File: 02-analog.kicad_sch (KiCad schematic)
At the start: 24 parts, among them J2 Superseal_1.0_5pol_MicA, J3 Superseal_1.0_5pol_MicB

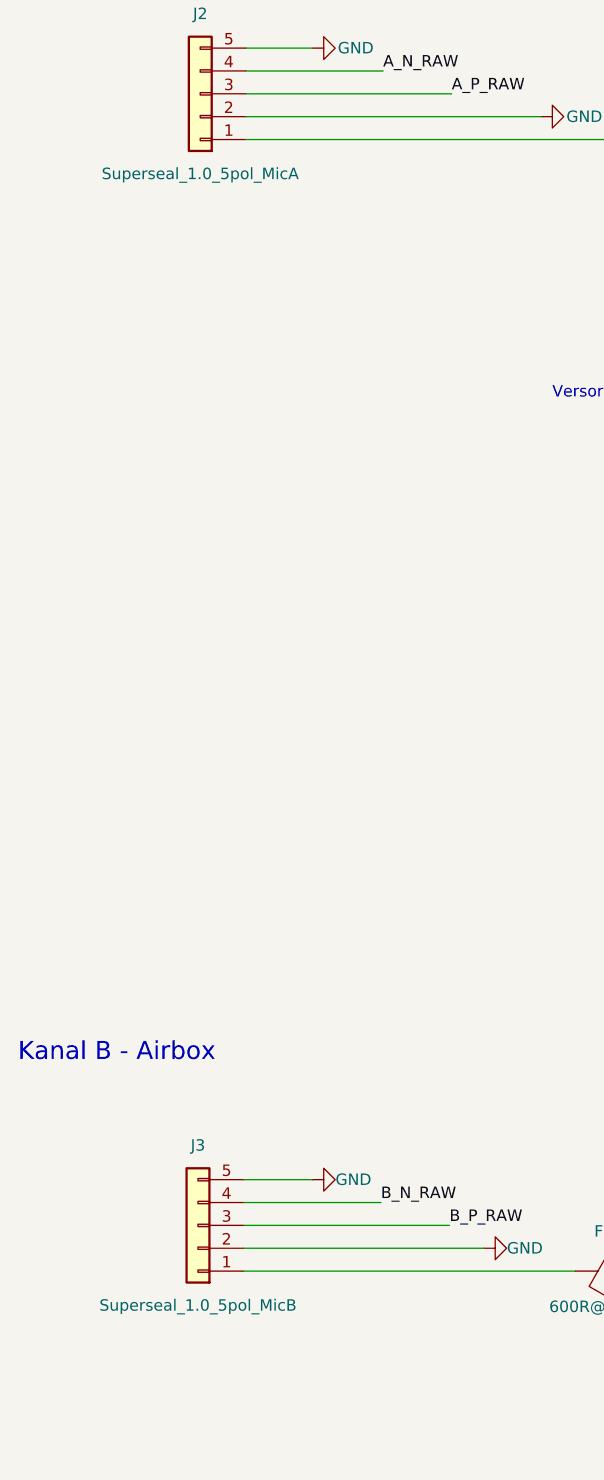
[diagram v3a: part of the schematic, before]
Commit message: Footprints im Schaltplan auf den Stand des Layouts ziehen
Neun Bauteile trugen im Schaltplan einen Footprint, der so nicht baubar ist.
Das Layout hatte sie laengst ersetzt; jetzt steht es auch im Schaltplan:

  U5      TSSOP-30 4,4 x 9,7 / 0,65  ->  4,4 x 7,8 / 0,5  (Datenblatt)
  U6      ESP32-S2-WROOM             ->  ESP32-S3-WROOM-1
  L2, L3  L_CommonModeChoke_WE-SL2   ->  L_CommonMode_WE-SL2
  J1..J3  TE Superseal 1.0           ->  JST XH liegend
  BT1     Keystone 3034 / CR2032     ->  Keystone 3000 / CR1220
  LS1     Piezo bedrahtet 12 mm      ->  Murata-Landmuster 9 x 9 mm SMD

Wo sich damit das Bauteil aendert, sind Wert und Bestellnummer mitgezogen.
Zwei Punkte dabei zum Nachlesen:

* BT1 hat mit CR1220 rund ein Viertel der Kapazitaet von CR2032. Die
  Platine ist fuer den 12-mm-Halter gebohrt, darum folgt der Schaltplan.
* Der im Layout benannte Murata PKMCS0909E ist abgekuendigt ("Last Time
  Buy") und nur fuer 1,5 V spezifiziert, angesteuert wird aber mit 3,3 V.
  Bestellt wird darum ein 3-V-Typ gleicher Bauform (Same Sky
  CPT-9019A-SMT-TR); das Landmuster gehoert gegen das Datenblatt geprueft.

Damit sind die Steckverbinder J1..J3 beschaffbar - Superseal 1.0 gibt es bei
DigiKey nur kabelseitig. Offen bleiben noch J4 und MK1.

Schaltplanparitaet: 18 -> 9 Abweichungen auf der Hauptplatine, 2 auf dem
Mikrofonkopf. Die restlichen sind keine Footprints mehr, sondern Symbole:
U2 hat einen Pin 4, den das SOT-223 nicht hat, und dem microSD-Symbol fehlt
der Schirmanschluss. Beides steht im README.

Die Stueckliste fuehrt jetzt eine Spalte Hinweis - dort landen die
Ersatzgruende, die vorher nur im Schaltplan standen.

DRC unveraendert: 0 Fehler, 10 Warnungen, 7 offene Verbindungen. ERC
unveraendert. Stuecklisten, Fertigungsdaten und PDFs neu erzeugt.
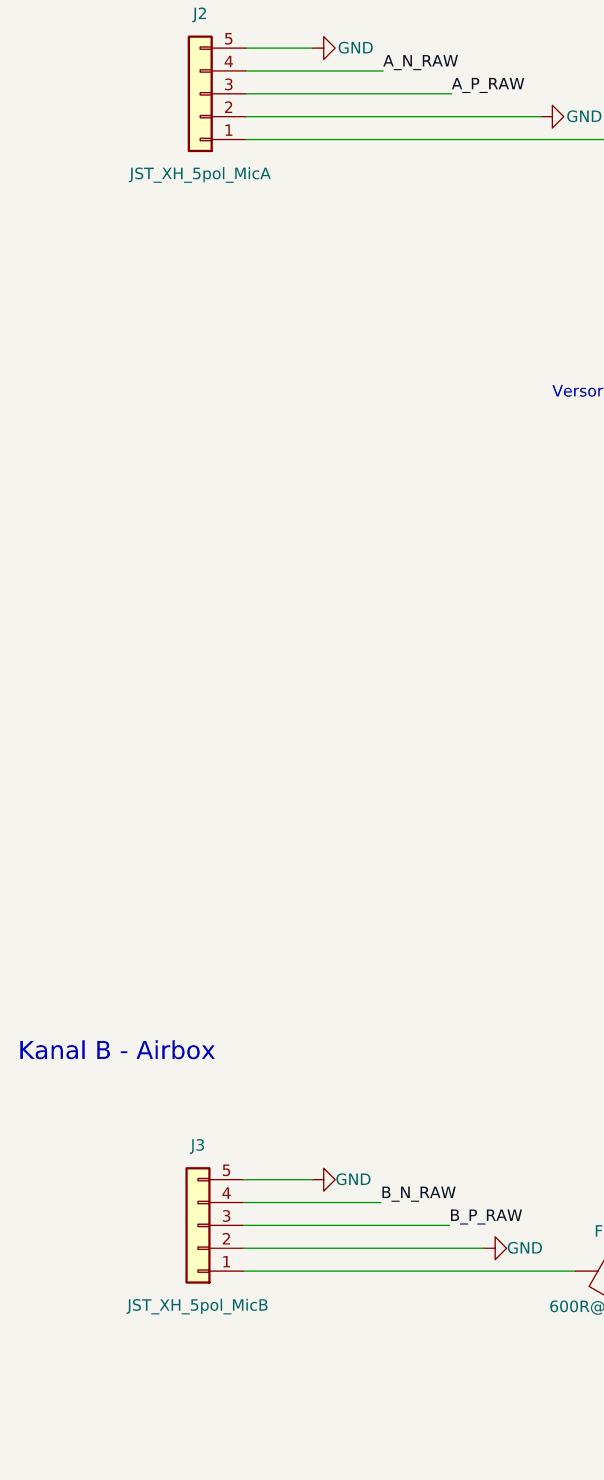
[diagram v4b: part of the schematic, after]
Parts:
- J2: value Superseal_1.0_5pol_MicA -> JST_XH_5pol_MicA; footprint Connector_TE:TE_Superseal_1.0_5way -> Connector_JST:JST_XH_S5B-XH-A_1x05_P2.50mm_Horizontal; DigiKey (none) -> 455-S5B-XH-A-ND; Hersteller (none) -> JST Sales America Inc.; Hinweis (none) -> Superseal 1.0 sitzt im Kabelbaum; auf der Platine JST XH; MPN (none) -> S5B-XH-A
- J3: value Superseal_1.0_5pol_MicB -> JST_XH_5pol_MicB; footprint Connector_TE:TE_Superseal_1.0_5way -> Connector_JST:JST_XH_S5B-XH-A_1x05_P2.50mm_Horizontal; DigiKey (none) -> 455-S5B-XH-A-ND; Hersteller (none) -> JST Sales America Inc.; Hinweis (none) -> Superseal 1.0 sitzt im Kabelbaum; auf der Platine JST XH; MPN (none) -> S5B-XH-A
- L2, L3: footprint Inductor_SMD:L_CommonModeChoke_Wuerth_WE-SL2 -> Inductor_SMD:L_CommonMode_Wuerth_WE-SL2
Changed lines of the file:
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@@
 			)
 		)
-		(property "Value" "Superseal_1.0_5pol_MicA"
+		(property "Value" "JST_XH_5pol_MicA"
 			(at 44.7 82.55 0)
 			(show_name no)
@@
 			)
 		)
-		(property "Footprint" "Connector_TE:TE_Superseal_1.0_5way"
+		(property "Footprint" "Connector_JST:JST_XH_S5B-XH-A_1x05_P2.50mm_Horizontal"
 			(at 44.7 73.66 0)
 			(hide yes)
@@
 		(property "Description" ""
 			(at 44.7 73.66 0)
+			(show_name no)
+			(do_not_autoplace no)
+			(effects
+				(font
+					(size 1.27 1.27)
+				)
+			)
+		)
+		(property "Hinweis" "Superseal 1.0 sitzt im Kabelbaum; auf der Platine JST XH"
+			(at 44.7 73.66 0)
+			(hide yes)
+			(show_name no)
+			(do_not_autoplace no)
+			(effects
+				(font
+					(size 1.27 1.27)
+				)
+			)
+		)
+		(property "MPN" "S5B-XH-A"
+			(at 44.7 73.66 0)
+			(hide yes)
+			(show_name no)
+			(do_not_autoplace no)
+			(effects
+				(font
+					(size 1.27 1.27)
+				)
+			)
+		)
+		(property "Hersteller" "JST Sales America Inc."
+			(at 44.7 73.66 0)
+			(hide yes)
+			(show_name no)
+			(do_not_autoplace no)
+			(effects
+				(font
+					(size 1.27 1.27)
+				)
+			)
+		)
+		(property "DigiKey" "455-S5B-XH-A-ND"
+			(at 44.7 73.66 0)
+			(hide yes)
 			(show_name no)
 			(do_not_autoplace no)
@@
 			)
 		)
-		(property "Footprint" "Inductor_SMD:L_CommonModeChoke_Wuerth_WE-SL2"
+		(property "Footprint" "Inductor_SMD:L_CommonMode_Wuerth_WE-SL2"
 			(at 228.6 85.09 0)
 			(hide yes)
@@
 			)
 		)
-		(property "Footprint" "Inductor_SMD:L_CommonModeChoke_Wuerth_WE-SL2"
+		(property "Footprint" "Inductor_SMD:L_CommonMode_Wuerth_WE-SL2"
 			(at 228.9 203.2 0)
 			(hide yes)
@@
 			)
 		)
-		(property "Value" "Superseal_1.0_5pol_MicB"
+		(property "Value" "JST_XH_5pol_MicB"
 			(at 44.45 208.28 0)
 			(show_name no)
@@
 			)
 		)
-		(property "Footprint" "Connector_TE:TE_Superseal_1.0_5way"
+		(property "Footprint" "Connector_JST:JST_XH_S5B-XH-A_1x05_P2.50mm_Horizontal"
 			(at 44.45 199.39 0)
 			(hide yes)
@@
 			(show_name no)
 			(do_not_autoplace no)
+			(effects
+				(font
+					(size 1.27 1.27)
+				)
+			)
+		)
+		(property "Hinweis" "Superseal 1.0 sitzt im Kabelbaum; auf der Platine JST XH"
+			(at 44.45 199.39 0)
+			(hide yes)
+			(show_name no)
+			(do_not_autoplace no)
+			(effects
+				(font
+					(size 1.27 1.27)
+				)
+			)
+		)
+		(property "MPN" "S5B-XH-A"
+			(at 44.45 199.39 0)
+			(hide yes)
+			(show_name no)
+			(do_not_autoplace no)
+			(effects
+				(font
+					(size 1.27 1.27)
+				)
+			)
+		)
+		(property "Hersteller" "JST Sales America Inc."
+			(at 44.45 199.39 0)
+			(hide yes)
+			(show_name no)
+			(do_not_autoplace no)
+			(effects
+				(font
+					(size 1.27 1.27)
+				)
+			)
+		)
+		(property "DigiKey" "455-S5B-XH-A-ND"
+			(at 44.45 199.39 0)
+			(hide yes)
+			(show_name no)
+			(do_not_autoplace no)
